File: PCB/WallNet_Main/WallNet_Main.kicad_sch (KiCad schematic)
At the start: 7 parts, among them J1 Conn_01x05_Pin, SW1 SW, U4 BT832

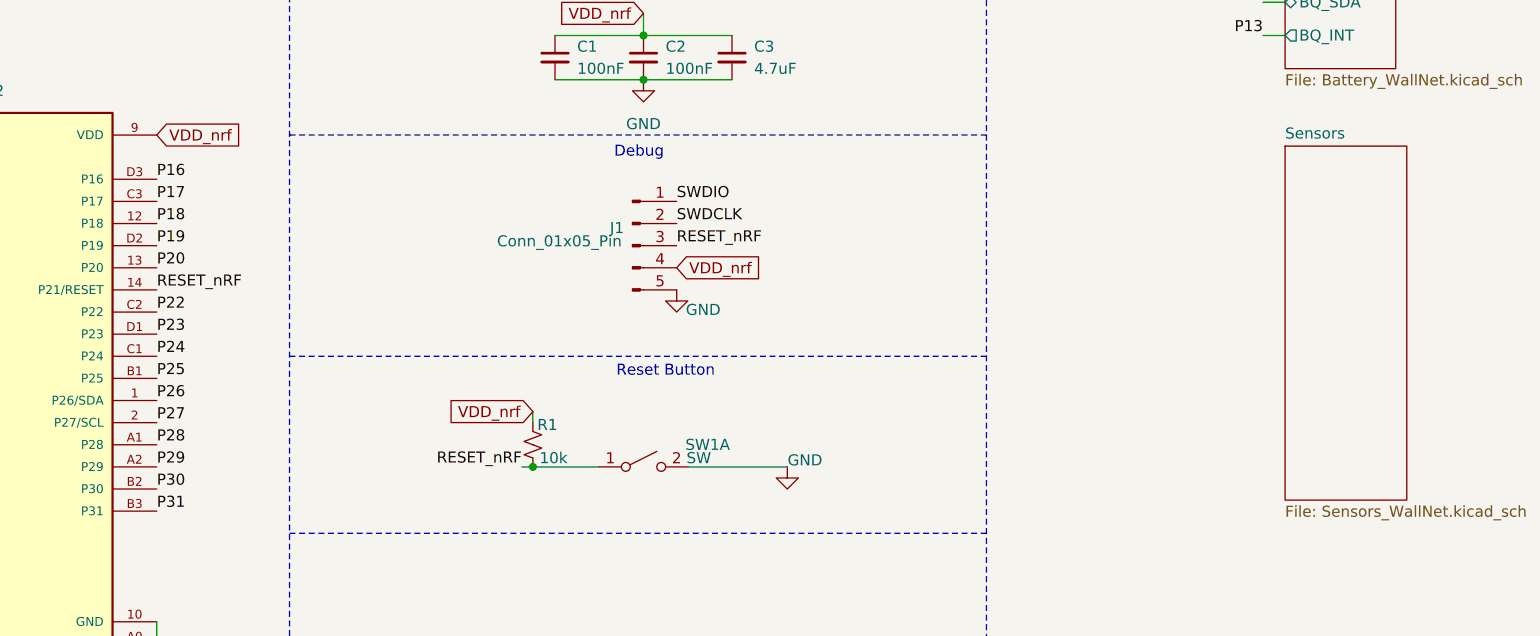
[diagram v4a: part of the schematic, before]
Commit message: E-ink & GPS connection Complete
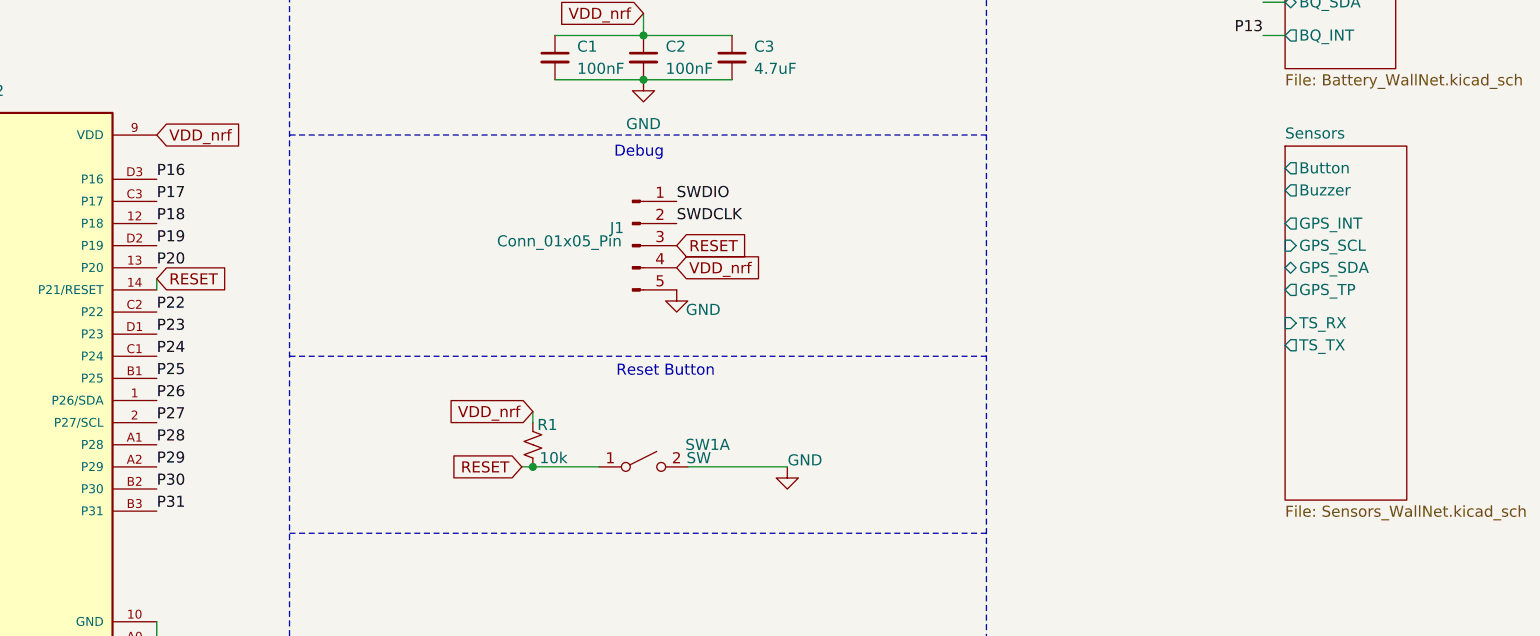
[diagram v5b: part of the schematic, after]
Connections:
- net RESET_nRF renamed RESET
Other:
- sheet Sensors ports: added Button, Buzzer, GPS_INT, GPS_SCL, GPS_SDA, GPS_TP, TS_RX, TS_TX; removed none

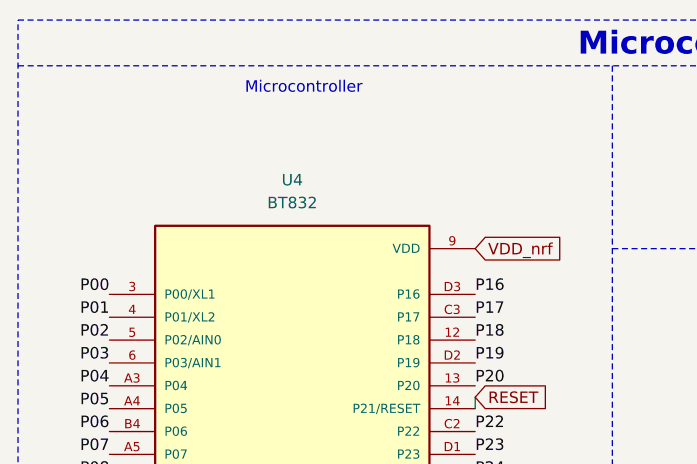
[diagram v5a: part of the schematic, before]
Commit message: Parts complete for schematic
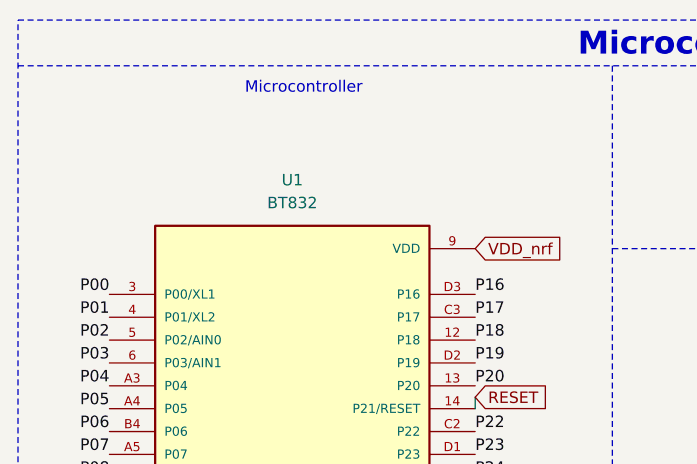
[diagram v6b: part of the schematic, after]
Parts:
- R1: footprint (none) -> Resistor_SMD:R_0201_0603Metric
- renumbered U4 to U1
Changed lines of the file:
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@@
 		(dnp no)
 		(fields_autoplaced yes)
-		(property "Reference" "U4"
+		(property "Reference" "U1"
 			(at 48.26 40.64 0)
 			(effects
@@
 			(project "WallNet_Main"
 				(path "/3272dd14-9e34-4275-b10b-c06dab1b3ca1"
-					(reference "U4")
+					(reference "U1")
 					(unit 1)
 				)
@@
 			)
 		)
-		(property "Footprint" ""
+		(property "Footprint" "Resistor_SMD:R_0201_0603Metric"
 			(at 111.76 83.82 0)
 			(effects

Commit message: Schematic done, updated layout
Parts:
- C1, C2: footprint Capacitor_SMD:C_0402_1005Metric -> Capacitor_SMD:C_0603_1608Metric
- C3: footprint Capacitor_SMD:C_0201_0603Metric -> Capacitor_SMD:C_0805_2012Metric
- R1: footprint Resistor_SMD:R_0201_0603Metric -> Resistor_SMD:R_0603_1608Metric
- SW1: footprint (none) -> Button_Switch_SMD:SW_Push_1P1T_NO_E-Switch_TL3301NxxxxxG
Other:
- sheet Sensors ports: added EP_BUSY, EP_CSB, EP_DC, EP_RESET, EP_SCL, EP_SDA, RFID_MISO, RFID_MOSI, RFID_RST, RFID_SCK, RFID_SS; removed none

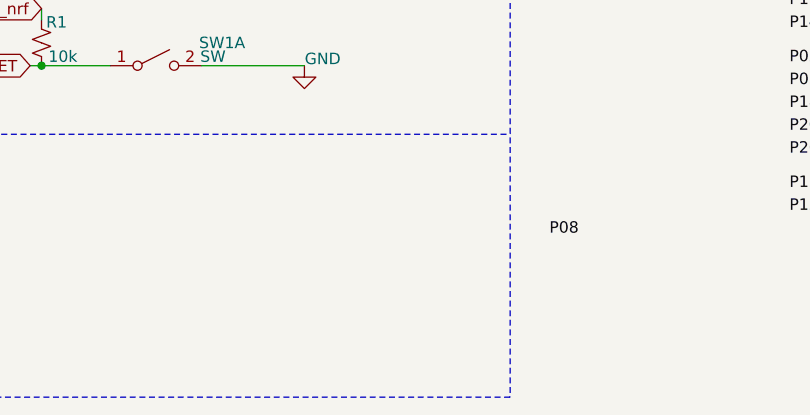
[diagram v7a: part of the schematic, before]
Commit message: added debug LED
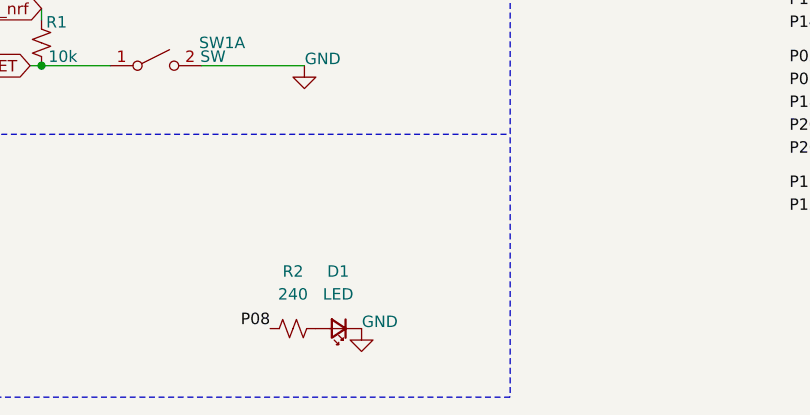
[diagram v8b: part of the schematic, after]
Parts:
- added D1: LED, Diode_SMD:D_0603_1608Metric, symbol Device:LED_Small
- added R2: 240, Resistor_SMD:R_0603_1608Metric, symbol Device:R_Small_US
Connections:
- net GND: now also D1.1 (K)
- net P08: now also R2.1
- new net: D1.2 (A), R2.2
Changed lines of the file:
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@@
 	)
 	(label "P08"
-		(at 171.45 105.41 180)
+		(at 137.16 115.57 180)
 		(effects
 			(font
@@
 				(justify right)
 				(hide yes)
+			)
+		)
+	)
+	(symbol
+		(lib_id "power:GND")
+		(at 147.32 115.57 0)
+		(unit 1)
+		(exclude_from_sim no)
+		(in_bom yes)
+		(on_board yes)
+		(dnp no)
+		(property "Reference" "#PWR031"
+			(at 147.32 121.92 0)
+			(effects
+				(font
+					(size 1.27 1.27)
+				)
+				(hide yes)
+			)
+		)
+		(property "Value" "GND"
+			(at 149.352 114.808 0)
+			(effects
+				(font
+					(size 1.27 1.27)
+				)
+			)
+		)
+		(property "Footprint" ""
+			(at 147.32 115.57 0)
+			(effects
+				(font
+					(size 1.27 1.27)
+				)
+				(hide yes)
+			)
+		)
+		(property "Datasheet" ""
+			(at 147.32 115.57 0)
+			(effects
+				(font
+					(size 1.27 1.27)
+				)
+				(hide yes)
+			)
+		)
+		(property "Description" "Power symbol creates a global label with name \"GND\" , ground"
+			(at 147.32 115.57 0)
+			(effects
+				(font
+					(size 1.27 1.27)
+				)
+				(hide yes)
+			)
+		)
+		(pin "1"
+		)
+		(instances
+			(project "WallNet_Main"
+				(path "/3272dd14-9e34-4275-b10b-c06dab1b3ca1"
+					(reference "#PWR031")
+					(unit 1)
+				)
 			)
 		)
@@
 	)
 	(symbol
+		(lib_id "Device:LED_Small")
+		(at 144.78 115.57 180)
+		(unit 1)
+		(exclude_from_sim no)
+		(in_bom yes)
+		(on_board yes)
+		(dnp no)
+		(fields_autoplaced yes)
+		(property "Reference" "D1"
+			(at 144.7165 109.22 0)
+			(effects
+				(font
+					(size 1.27 1.27)
+				)
+			)
+		)
+		(property "Value" "LED"
+			(at 144.7165 111.76 0)
+			(effects
+				(font
+					(size 1.27 1.27)
+				)
+			)
+		)
+		(property "Footprint" "Diode_SMD:D_0603_1608Metric"
+			(at 144.78 115.57 90)
+			(effects
+				(font
+					(size 1.27 1.27)
+				)
+				(hide yes)
+			)
+		)
+		(property "Datasheet" "~"
+			(at 144.78 115.57 90)
+			(effects
+				(font
+					(size 1.27 1.27)
+				)
+				(hide yes)
+			)
+		)
+		(property "Description" "Light emitting diode, small symbol"
+			(at 144.78 115.57 0)
+			(effects
+				(font
+					(size 1.27 1.27)
+				)
+				(hide yes)
+			)
+		)
+		(property "Sim.Pins" "1=K 2=A"
+			(at 144.78 115.57 0)
+			(effects
+				(font
+					(size 1.27 1.27)
+				)
+				(hide yes)
+			)
+		)
+		(pin "1"
+		)
+		(pin "2"
+		)
+		(instances
+			(project "WallNet_Main"
+				(path "/3272dd14-9e34-4275-b10b-c06dab1b3ca1"
+					(reference "D1")
+					(unit 1)
+				)
+			)
+		)
+	)
+	(symbol
 		(lib_id "Switch:SW_DPST_x2")
 		(at 124.46 86.36 0)
@@
 					(unit 1)
 				)
+			)
+		)
+	)
+	(symbol
+		(lib_id "Device:R_Small_US")
+		(at 139.7 115.57 90)
+		(unit 1)
+		(exclude_from_sim no)
+		(in_bom yes)
+		(on_board yes)
+		(dnp no)
+		(fields_autoplaced yes)
+		(property "Reference" "R2"
+			(at 139.7 109.22 90)
+			(effects
+				(font
+					(size 1.27 1.27)
+				)
+			)
+		)
+		(property "Value" "240"
+			(at 139.7 111.76 90)
+			(effects
+				(font
+					(size 1.27 1.27)
+				)
+			)
+		)
+		(property "Footprint" "Resistor_SMD:R_0603_1608Metric"
+			(at 139.7 115.57 0)
+			(effects
+				(font
+					(size 1.27 1.27)
+				)
+				(hide yes)
+			)
+		)
+		(property "Datasheet" "~"
+			(at 139.7 115.57 0)
+			(effects
+				(font
+					(size 1.27 1.27)
+				)
+				(hide yes)
+			)
+		)
+		(property "Description" "Resistor, small US symbol"
+			(at 139.7 115.57 0)
+			(effects
+				(font
+					(size 1.27 1.27)
+				)
+				(hide yes)
+			)
+		)
+		(pin "1"
+		)
+		(pin "2"
+		)
+		(instances
+			(project ""
+				(path "/3272dd14-9e34-4275-b10b-c06dab1b3ca1"
+					(reference "R2")
+					(unit 1)
+				)
